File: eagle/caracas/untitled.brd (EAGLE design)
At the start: 100 x 80 mm, 12 parts, among them IC1 ICM7555

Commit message: Update Eagle project.
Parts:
- removed R4: 10k, rcl:0204/7
- IC1: value ICM7555 -> 4027N; device maxim:DIL08 -> 40xx:DIL16
- moved C2 155.1 mm to (-21.6, 69.8)
- moved C1 150.3 mm to (-16.5, 69.8)
- moved D1 107.5 mm to (-50.8, 57.1)
- moved CON1 99.4 mm to (-33.0, 44.5)
- moved T1 96.3 mm to (-40.6, 57.1)
- moved R2 86.8 mm to (-43.2, 67.3)
- moved U$1 78.0 mm to (-31.8, 11.4)
- moved IC1 73.3 mm to (-24.1, 59.7)
- moved R1 66.3 mm to (-30.5, 67.3)
- moved R3 66.3 mm to (-19.1, 74.9)
- moved X1 61.0 mm to (-21.6, 22.9)
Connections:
- removed net VCC: C1.1, C2.2, IC1.4, IC1.8, U$1.+VIN1, U$1.+VIN2, U$1.+VOUT
- new net +12V: C2.2, U$1.+VIN1, U$1.+VIN2
- new net +12V_IGN: R3.1
- new net +5V: C1.1, U$1.+VOUT
- new net VDD: IC1.16
- new net VSS: IC1.8
- net GND: no longer IC1.1, R4.1
- net N$1: now also IC1.7, R3.2; no longer IC1.3, R4.2, U$1.CONTROL
- net RPI-OFFSIGNAL: now also IC1.4; no longer IC1.2, IC1.6
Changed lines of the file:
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@@
 <pass name="Default">
 <param name="RoutingGrid" value="50mil"/>
-<param name="tpViaShape" value="octagon"/>
+<param name="tpViaShape" value="round"/>
 <param name="PrefDir.1" value="|"/>
 <param name="PrefDir.2" value="0"/>
@@
 </autorouter>
 <elements>
-<element name="R1" library="rcl" package="0207/10" value="" x="33.02" y="48.26"/>
-<element name="R2" library="rcl" package="0207/10" value="" x="39.37" y="40.64"/>
-<element name="R3" library="rcl" package="0207/10" value="" x="43.18" y="52.07"/>
-<element name="IC1" library="maxim" package="DIL08" value="ICM7555" x="7.62" y="-6.35">
-<attribute name="OC_NEWARK" value="68K4387" x="7.62" y="-6.35" size="1.778" layer="27" display="off"/>
-<attribute name="MPN" value="ICM7555IPA+" x="7.62" y="-6.35" size="1.778" layer="27" display="off"/>
-<attribute name="MF" value="MAXIM" x="7.62" y="-6.35" size="1.778" layer="27" display="off"/>
-<attribute name="OC_FARNELL" value="9663762" x="7.62" y="-6.35" size="1.778" layer="27" display="off"/>
+<element name="R1" library="rcl" package="0207/10" value="" x="-30.48" y="67.31"/>
+<element name="R2" library="rcl" package="0207/10" value="" x="-43.18" y="67.31"/>
+<element name="R3" library="rcl" package="0207/10" value="" x="-19.05" y="74.93"/>
+<element name="X1" library="con-yamaichi" package="USB-A003" value="" x="-21.59" y="22.86">
+<attribute name="OC_NEWARK" value="unknown" x="0" y="0" size="1.778" layer="27" display="off"/>
+<attribute name="MPN" value="" x="0" y="0" size="1.778" layer="27" display="off"/>
+<attribute name="MF" value="" x="0" y="0" size="1.778" layer="27" display="off"/>
+<attribute name="OC_FARNELL" value="unknown" x="0" y="0" size="1.778" layer="27" display="off"/>
 </element>
-<element name="X1" library="con-yamaichi" package="USB-A003" value="" x="10.16" y="-29.21">
-<attribute name="OC_NEWARK" value="unknown" x="10.16" y="-29.21" size="1.778" layer="27" display="off"/>
-<attribute name="MPN" value="" x="10.16" y="-29.21" size="1.778" layer="27" display="off"/>
-<attribute name="MF" value="" x="10.16" y="-29.21" size="1.778" layer="27" display="off"/>
-<attribute name="OC_FARNELL" value="unknown" x="10.16" y="-29.21" size="1.778" layer="27" display="off"/>
+<element name="CON1" library="con-harting" package="CON26" value="" x="-33.02" y="44.45">
+<attribute name="OC_NEWARK" value="unknown" x="0" y="0" size="1.778" layer="27" display="off"/>
+<attribute name="MPN" value="" x="0" y="0" size="1.778" layer="27" display="off"/>
+<attribute name="MF" value="" x="0" y="0" size="1.778" layer="27" display="off"/>
+<attribute name="OC_FARNELL" value="unknown" x="0" y="0" size="1.778" layer="27" display="off"/>
 </element>
-<element name="CON1" library="con-harting" package="CON26" value="" x="20.32" y="-39.37">
-<attribute name="OC_NEWARK" value="unknown" x="20.32" y="-39.37" size="1.778" layer="27" display="off"/>
-<attribute name="MPN" value="" x="20.32" y="-39.37" size="1.778" layer="27" display="off"/>
-<attribute name="MF" value="" x="20.32" y="-39.37" size="1.778" layer="27" display="off"/>
-<attribute name="OC_FARNELL" value="unknown" x="20.32" y="-39.37" size="1.778" layer="27" display="off"/>
-</element>
-<element name="T1" library="transistor-neu-to92" package="TO92-EBC" value="" x="-26.67" y="-38.1"/>
-<element name="D1" library="diode" package="DO41-10" value="1N4004" x="-24.13" y="-46.99"/>
-<element name="U$1" library="caracas" package="NCS12S1205C" value="NCS12S1205C" x="45.72" y="20.32"/>
-<element name="R4" library="rcl" package="0204/7" value="10k" x="-25.4" y="-74.93"/>
-<element name="C1" library="rcl" package="C025-024X044" value="220µ" x="-27.94" y="-80.01"/>
-<element name="C2" library="rcl" package="C025-024X044" value="10µ" x="-27.94" y="-85.09"/>
+<element name="T1" library="transistor-neu-to92" package="TO92-EBC" value="" x="-40.64" y="57.15"/>
+<element name="D1" library="diode" package="DO41-10" value="1N4004" x="-50.8" y="57.15"/>
+<element name="U$1" library="caracas" package="NCS12S1205C" value="NCS12S1205C" x="-31.75" y="11.43"/>
+<element name="C1" library="rcl" package="C025-024X044" value="220µ" x="-16.51" y="69.85"/>
+<element name="C2" library="rcl" package="C025-024X044" value="10µ" x="-21.59" y="69.85"/>
+<element name="IC1" library="40xx" package="DIL16" value="4027N" x="-24.13" y="59.69"/>
 </elements>
 <signals>
+<signal name="VSS">
+<contactref element="IC1" pad="8"/>
+</signal>
+<signal name="VDD">
+<contactref element="IC1" pad="16"/>
+</signal>
 <signal name="GND">
-<contactref element="R4" pad="1"/>
+<contactref element="C2" pad="1"/>
 <contactref element="U$1" pad="0V"/>
 <contactref element="C1" pad="2"/>
+<contactref element="U$1" pad="-VIN1"/>
 <contactref element="U$1" pad="-VIN2"/>
-<contactref element="U$1" pad="-VIN1"/>
-<contactref element="C2" pad="1"/>
-<contactref element="IC1" pad="1"/>
-<wire x1="-26.67" y1="-80.01" x2="-29.21" y2="-85.09" width="0" layer="19" extent="1-1"/>
-<wire x1="-29.21" y1="-74.93" x2="-26.67" y2="-80.01" width="0" layer="19" extent="1-1"/>
-<wire x1="35.56" y1="12.7" x2="-29.21" y2="-74.93" width="0" layer="19" extent="1-1"/>
-<wire x1="38.1" y1="12.7" x2="35.56" y2="12.7" width="0" layer="19" extent="1-1"/>
-<wire x1="53.34" y1="27.94" x2="38.1" y2="12.7" width="0" layer="19" extent="1-1"/>
-<wire x1="3.81" y1="-10.16" x2="53.34" y2="27.94" width="0" layer="19" extent="1-1"/>
+<wire x1="-22.86" y1="69.85" x2="-15.24" y2="69.85" width="0" layer="19" extent="1-1"/>
+<wire x1="-24.13" y1="19.05" x2="-22.86" y2="69.85" width="0" layer="19" extent="1-1"/>
+<wire x1="-39.37" y1="3.81" x2="-24.13" y2="19.05" width="0" layer="19" extent="1-1"/>
+<wire x1="-41.91" y1="3.81" x2="-39.37" y2="3.81" width="0" layer="19" extent="1-1"/>
 </signal>
-<signal name="N$1">
-<contactref element="IC1" pad="3"/>
-<contactref element="U$1" pad="CONTROL"/>
-<contactref element="R4" pad="2"/>
-<wire x1="-21.59" y1="-74.93" x2="33.02" y2="12.7" width="0" layer="19" extent="1-1"/>
-<wire x1="8.89" y1="-10.16" x2="33.02" y2="12.7" width="0" layer="19" extent="1-1"/>
-</signal>
-<signal name="VCC">
+<signal name="+5V">
 <contactref element="C1" pad="1"/>
 <contactref element="U$1" pad="+VOUT"/>
-<contactref element="IC1" pad="8"/>
-<contactref element="C2" pad="2"/>
-<contactref element="U$1" pad="+VIN2"/>
-<contactref element="U$1" pad="+VIN1"/>
-<contactref element="IC1" pad="4"/>
-<wire x1="-29.21" y1="-80.01" x2="-26.67" y2="-85.09" width="0" layer="19" extent="1-1"/>
-<wire x1="11.43" y1="-10.16" x2="-29.21" y2="-80.01" width="0" layer="19" extent="1-1"/>
-<wire x1="3.81" y1="-2.54" x2="11.43" y2="-10.16" width="0" layer="19" extent="1-1"/>
-<wire x1="35.56" y1="27.94" x2="3.81" y2="-2.54" width="0" layer="19" extent="1-1"/>
-<wire x1="38.1" y1="27.94" x2="35.56" y2="27.94" width="0" layer="19" extent="1-1"/>
-<wire x1="58.42" y1="27.94" x2="38.1" y2="27.94" width="0" layer="19" extent="1-1"/>
+<wire x1="-19.05" y1="19.05" x2="-17.78" y2="69.85" width="0" layer="19" extent="1-1"/>
 </signal>
 <signal name="RPI-OFFSIGNAL">
 <contactref element="CON1" pad="10"/>
-<contactref element="IC1" pad="2"/>
-<contactref element="IC1" pad="6"/>
-<wire x1="6.35" y1="-10.16" x2="15.24" y2="-38.1" width="0" layer="19" extent="1-1"/>
-<wire x1="8.89" y1="-2.54" x2="6.35" y2="-10.16" width="0" layer="19" extent="1-1"/>
+<contactref element="IC1" pad="4"/>
+<wire x1="-38.1" y1="45.72" x2="-25.4" y2="55.88" width="0" layer="19" extent="1-1"/>
+</signal>
+<signal name="N$1">
+<contactref element="R3" pad="2"/>
+<contactref element="IC1" pad="7"/>
+<wire x1="-17.78" y1="55.88" x2="-13.97" y2="74.93" width="0" layer="19" extent="1-1"/>
+</signal>
+<signal name="+12V_IGN">
+<contactref element="R3" pad="1"/>
+</signal>
+<signal name="+12V">
+<contactref element="C2" pad="2"/>
+<contactref element="U$1" pad="+VIN1"/>
+<contactref element="U$1" pad="+VIN2"/>
+<wire x1="-39.37" y1="19.05" x2="-20.32" y2="69.85" width="0" layer="19" extent="1-1"/>
+<wire x1="-41.91" y1="19.05" x2="-39.37" y2="19.05" width="0" layer="19" extent="1-1"/>
 </signal>
 </signals>

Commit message: Update Eagle schematics.
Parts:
- removed D1: 1N4004, diode:DO41-10
- removed R2: (no value), rcl:0207/10
- removed T1: (no value), transistor-neu-to92:TO92-EBC
- removed X1: (no value), con-yamaichi:USB-A003
- added R4: (no value), rcl:0207/10
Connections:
- new net N$2: IC1.4, R4.2
- new net N$3: CON1.16, R1.2
- new net POWER_STATE: IC1.1, U$1.CONTROL
- net +5V: now also CON1.2, CON1.4
- net GND: now also CON1.6
- net RPI-OFFSIGNAL: now also CON1.18, R4.1; no longer CON1.10, IC1.4
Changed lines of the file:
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@@
 <elements>
 <element name="R1" library="rcl" package="0207/10" value="" x="-30.48" y="67.31"/>
-<element name="R2" library="rcl" package="0207/10" value="" x="-43.18" y="67.31"/>
 <element name="R3" library="rcl" package="0207/10" value="" x="-19.05" y="74.93"/>
-<element name="X1" library="con-yamaichi" package="USB-A003" value="" x="-21.59" y="22.86">
-<attribute name="OC_NEWARK" value="unknown" x="0" y="0" size="1.778" layer="27" display="off"/>
-<attribute name="MPN" value="" x="0" y="0" size="1.778" layer="27" display="off"/>
-<attribute name="MF" value="" x="0" y="0" size="1.778" layer="27" display="off"/>
-<attribute name="OC_FARNELL" value="unknown" x="0" y="0" size="1.778" layer="27" display="off"/>
-</element>
 <element name="CON1" library="con-harting" package="CON26" value="" x="-33.02" y="44.45">
 <attribute name="OC_NEWARK" value="unknown" x="0" y="0" size="1.778" layer="27" display="off"/>
@@
 <attribute name="OC_FARNELL" value="unknown" x="0" y="0" size="1.778" layer="27" display="off"/>
 </element>
-<element name="T1" library="transistor-neu-to92" package="TO92-EBC" value="" x="-40.64" y="57.15"/>
-<element name="D1" library="diode" package="DO41-10" value="1N4004" x="-50.8" y="57.15"/>
 <element name="U$1" library="caracas" package="NCS12S1205C" value="NCS12S1205C" x="-31.75" y="11.43"/>
 <element name="C1" library="rcl" package="C025-024X044" value="220µ" x="-16.51" y="69.85"/>
 <element name="C2" library="rcl" package="C025-024X044" value="10µ" x="-21.59" y="69.85"/>
 <element name="IC1" library="40xx" package="DIL16" value="4027N" x="-24.13" y="59.69"/>
+<element name="R4" library="rcl" package="0207/10" value="" x="-50.8" y="-3.81"/>
 </elements>
 <signals>
@@
 <contactref element="U$1" pad="-VIN1"/>
 <contactref element="U$1" pad="-VIN2"/>
+<contactref element="CON1" pad="6"/>
 <wire x1="-22.86" y1="69.85" x2="-15.24" y2="69.85" width="0" layer="19" extent="1-1"/>
-<wire x1="-24.13" y1="19.05" x2="-22.86" y2="69.85" width="0" layer="19" extent="1-1"/>
+<wire x1="-43.18" y1="45.72" x2="-22.86" y2="69.85" width="0" layer="19" extent="1-1"/>
+<wire x1="-24.13" y1="19.05" x2="-43.18" y2="45.72" width="0" layer="19" extent="1-1"/>
 <wire x1="-39.37" y1="3.81" x2="-24.13" y2="19.05" width="0" layer="19" extent="1-1"/>
 <wire x1="-41.91" y1="3.81" x2="-39.37" y2="3.81" width="0" layer="19" extent="1-1"/>
@@
 <contactref element="C1" pad="1"/>
 <contactref element="U$1" pad="+VOUT"/>
-<wire x1="-19.05" y1="19.05" x2="-17.78" y2="69.85" width="0" layer="19" extent="1-1"/>
+<contactref element="CON1" pad="2"/>
+<contactref element="CON1" pad="4"/>
+<wire x1="-45.72" y1="45.72" x2="-17.78" y2="69.85" width="0" layer="19" extent="1-1"/>
+<wire x1="-48.26" y1="45.72" x2="-45.72" y2="45.72" width="0" layer="19" extent="1-1"/>
+<wire x1="-19.05" y1="19.05" x2="-45.72" y2="45.72" width="0" layer="19" extent="1-1"/>
 </signal>
 <signal name="RPI-OFFSIGNAL">
-<contactref element="CON1" pad="10"/>
-<contactref element="IC1" pad="4"/>
-<wire x1="-38.1" y1="45.72" x2="-25.4" y2="55.88" width="0" layer="19" extent="1-1"/>
+<contactref element="R4" pad="1"/>
+<contactref element="CON1" pad="18"/>
+<wire x1="-27.94" y1="45.72" x2="-55.88" y2="-3.81" width="0" layer="19" extent="1-1"/>
 </signal>
 <signal name="N$1">
@@
 <wire x1="-41.91" y1="19.05" x2="-39.37" y2="19.05" width="0" layer="19" extent="1-1"/>
 </signal>
+<signal name="N$2">
+<contactref element="R4" pad="2"/>
+<contactref element="IC1" pad="4"/>
+<wire x1="-25.4" y1="55.88" x2="-45.72" y2="-3.81" width="0" layer="19" extent="1-1"/>
+</signal>
+<signal name="POWER_STATE">
+<contactref element="IC1" pad="1"/>
+<contactref element="U$1" pad="CONTROL"/>
+<wire x1="-33.02" y1="55.88" x2="-44.45" y2="3.81" width="0" layer="19" extent="1-1"/>
+</signal>
+<signal name="N$3">
+<contactref element="R1" pad="2"/>
+<contactref element="CON1" pad="16"/>
+<wire x1="-30.48" y1="45.72" x2="-25.4" y2="67.31" width="0" layer="19" extent="1-1"/>
+</signal>
 </signals>

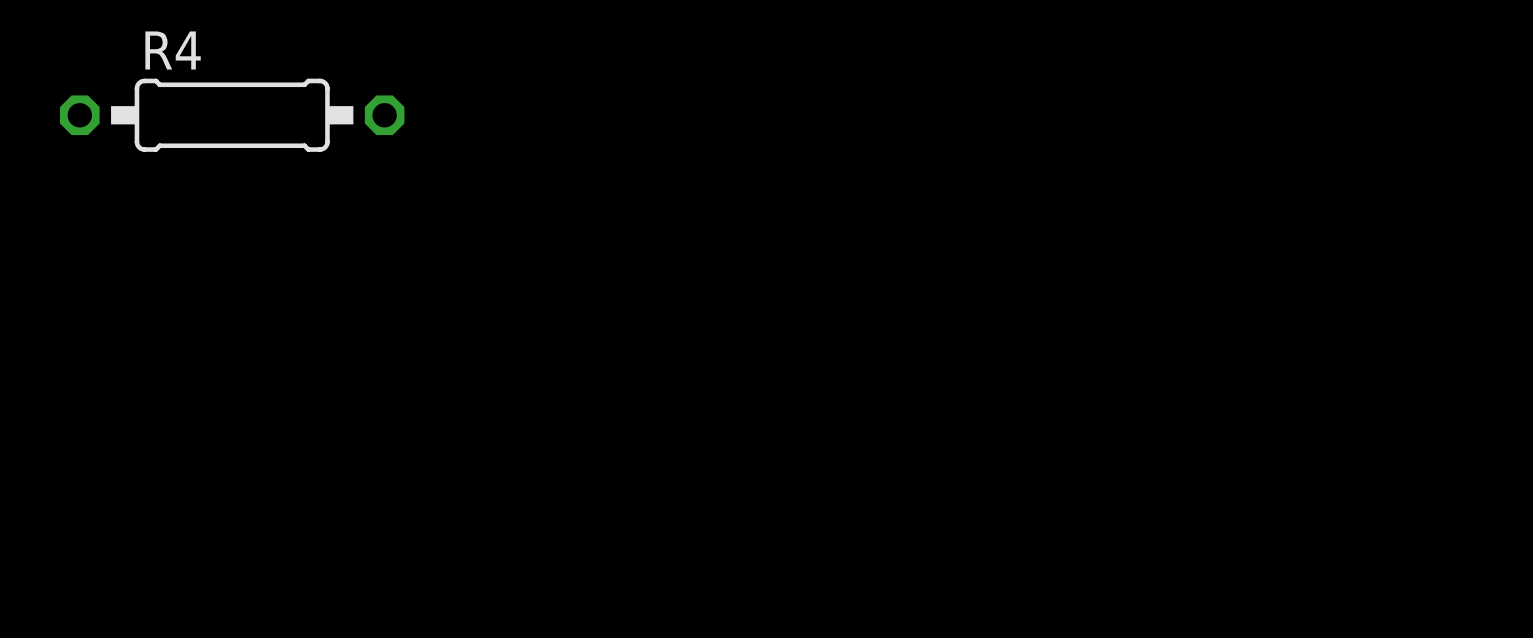
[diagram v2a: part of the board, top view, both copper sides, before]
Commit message: EAGLE: draw SATA connector into schematics.
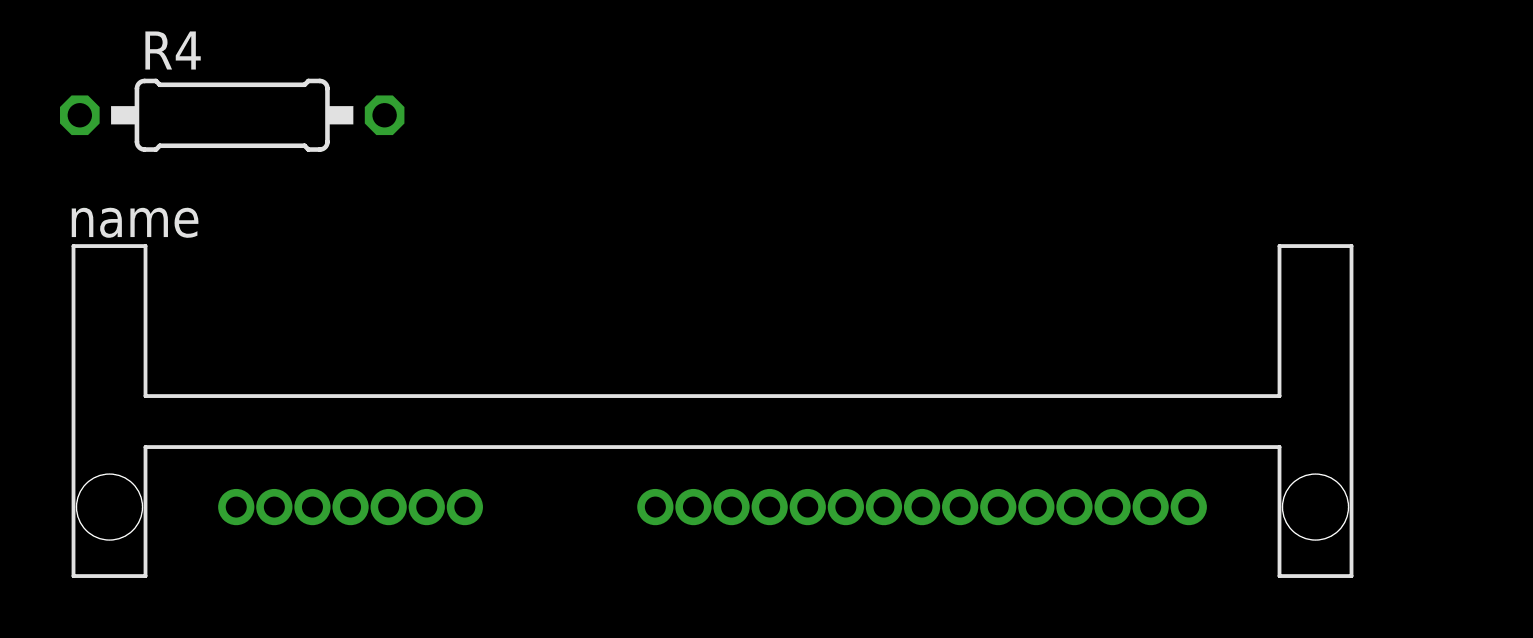
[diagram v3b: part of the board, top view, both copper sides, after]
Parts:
- added U$2: CD2109, caracas:CD2109
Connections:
- new net VCC: U$2.P7, U$2.P8, U$2.P9
- net GND: now also U$2.P10, U$2.P12, U$2.P4, U$2.P5, U$2.P6
- net POWER_STATE: now also R1.1
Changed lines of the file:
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@@
 <element name="IC1" library="40xx" package="DIL16" value="4027N" x="-24.13" y="59.69"/>
 <element name="R4" library="rcl" package="0207/10" value="" x="-50.8" y="-3.81"/>
+<element name="U$2" library="caracas" package="CD2109" value="CD2109" x="-34.29" y="-13.97"/>
 </elements>
 <signals>
@@
 <contactref element="U$1" pad="-VIN2"/>
 <contactref element="CON1" pad="6"/>
+<contactref element="U$2" pad="P4"/>
+<contactref element="U$2" pad="P5"/>
+<contactref element="U$2" pad="P6"/>
+<contactref element="U$2" pad="P10"/>
+<contactref element="U$2" pad="P12"/>
 <wire x1="-22.86" y1="69.85" x2="-15.24" y2="69.85" width="0" layer="19" extent="1-1"/>
 <wire x1="-43.18" y1="45.72" x2="-22.86" y2="69.85" width="0" layer="19" extent="1-1"/>
@@
 <wire x1="-39.37" y1="3.81" x2="-24.13" y2="19.05" width="0" layer="19" extent="1-1"/>
 <wire x1="-41.91" y1="3.81" x2="-39.37" y2="3.81" width="0" layer="19" extent="1-1"/>
+<wire x1="-32.885" y1="-16.87" x2="-39.37" y2="3.81" width="0" layer="19" extent="1-1"/>
+<wire x1="-31.615" y1="-16.87" x2="-32.885" y2="-16.87" width="0" layer="19" extent="1-1"/>
+<wire x1="-30.345" y1="-16.87" x2="-31.615" y2="-16.87" width="0" layer="19" extent="1-1"/>
+<wire x1="-25.265" y1="-16.87" x2="-30.345" y2="-16.87" width="0" layer="19" extent="1-1"/>
+<wire x1="-22.725" y1="-16.87" x2="-25.265" y2="-16.87" width="0" layer="19" extent="1-1"/>
 </signal>
 <signal name="+5V">
@@
 <contactref element="IC1" pad="1"/>
 <contactref element="U$1" pad="CONTROL"/>
+<contactref element="R1" pad="1"/>
 <wire x1="-33.02" y1="55.88" x2="-44.45" y2="3.81" width="0" layer="19" extent="1-1"/>
+<wire x1="-35.56" y1="67.31" x2="-33.02" y2="55.88" width="0" layer="19" extent="1-1"/>
 </signal>
 <signal name="N$3">
@@
 <wire x1="-30.48" y1="45.72" x2="-25.4" y2="67.31" width="0" layer="19" extent="1-1"/>
 </signal>
+<signal name="VCC">
+<contactref element="U$2" pad="P7"/>
+<contactref element="U$2" pad="P8"/>
+<contactref element="U$2" pad="P9"/>
+<wire x1="-27.805" y1="-16.87" x2="-29.075" y2="-16.87" width="0" layer="19" extent="1-1"/>
+<wire x1="-26.535" y1="-16.87" x2="-27.805" y2="-16.87" width="0" layer="19" extent="1-1"/>
+</signal>
 </signals>

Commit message: Finished design?
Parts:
- removed R3, R4: (no value), rcl:0207/10
- added U$3: MKDS3, caracas:MKDS3
- R1: value (none) -> 10k
- moved CON1 114.1 mm to (78.7, 21.6), turned to 90 degrees
- moved R1 91.7 mm to (48.3, 20.3), turned to 270 degrees
- moved U$2 85.3 mm to (48.3, 7.62), turned to 180 degrees
- moved IC1 84.8 mm to (57.1, 35.6)
- moved C1 64.8 mm to (20.3, 16.5), turned to 90 degrees
- moved C2 64.8 mm to (15.2, 16.5), turned to 90 degrees
- moved U$1 53.1 mm to (17.8, 30.5)
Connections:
- removed net +12V: C2.2, U$1.+VIN1, U$1.+VIN2
- removed net N$1: IC1.7, R3.2
- removed net N$2: IC1.4, R4.2
- removed net VDD: IC1.16
- removed net VSS: IC1.8
- net +12V_IGN: now also IC1.7, U$3.P$2; no longer R3.1
- net +5V: now also U$2.P7, U$2.P8, U$2.P9, U$3.P$3
- net GND: now also IC1.3, IC1.5, IC1.6, IC1.8, U$3.P$4
- net RPI-OFFSIGNAL: now also IC1.4; no longer R4.1
- net VCC: now also C2.2, IC1.16, U$1.+VIN1, U$1.+VIN2, U$3.P$1; no longer U$2.P7, U$2.P8, U$2.P9
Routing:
- net +5V: track 0.00 -> 211.4 mm
- net GND: track 0.00 -> 170.1 mm
- net +12V_IGN: track 0.00 -> 94.1 mm
- net VCC: track 0.00 -> 85.4 mm
- net POWER_STATE: track 0.00 -> 59.5 mm
- net N$3: track 0.00 -> 32.9 mm
- net RPI-OFFSIGNAL: track 0.00 -> 23.7 mm
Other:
- board size 100 x 80 mm -> 84.8 x 43.2 mm
